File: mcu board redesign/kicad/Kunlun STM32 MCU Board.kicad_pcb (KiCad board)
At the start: 2 copper layers, 40 x 40 mm, 36 parts, among them J1 0532610671, J2 10129383-908001ALF, J3 USB4105-GF-A, J4 5002, J5 5002, J6 5002, J7 5002, J8 5001, J9 5001, SW1 KMR231NG ULC LFS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

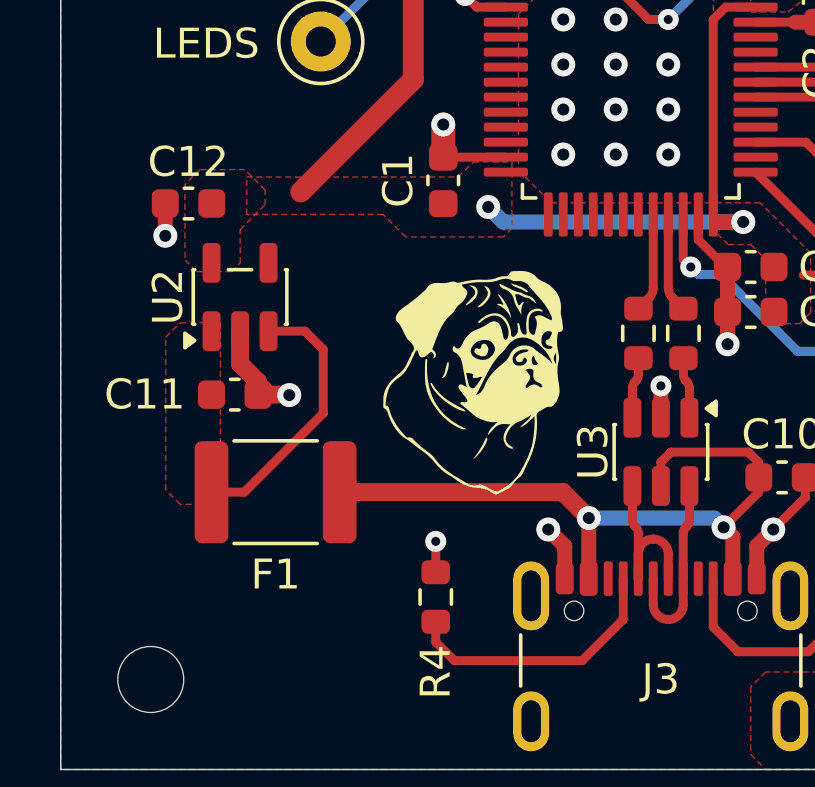
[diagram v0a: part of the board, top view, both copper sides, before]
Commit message: Added speaker, changed fuse.
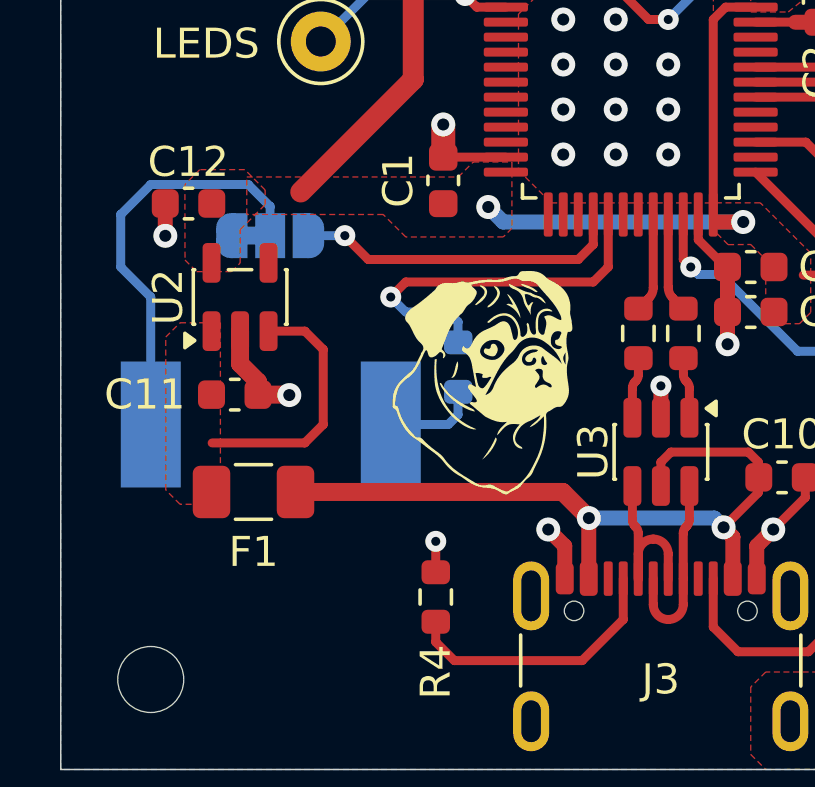
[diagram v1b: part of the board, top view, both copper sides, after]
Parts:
- added JP1: SolderJumper_3_Bridged12, Jumper:SolderJumper-3_P1.3mm_Bridged12_RoundedPad1.0x1.5mm, B.Cu at (135.2, 107.0)
- added LS1: Speaker, Buzzer_Beeper:Buzzer_CUI_CPT-9019S-SMT, B.Cu at (135.2, 113.2)
- added R7: 100, Resistor_SMD:R_0603_1608Metric, B.Cu at (141.5, 111.3)
- F1: footprint Fuse:Fuse_1812_4532Metric -> Fuse:Fuse_1206_3216Metric
- moved F1 0.74 mm to (134.7, 115.5)
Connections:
- U1 pad 28: unconnected-(U1-PB15-Pad28) -> /SPKR_ALT
- U1 pad 29: unconnected-(U1-PA8-Pad29) -> /SPKR_OUT
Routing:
- net Net-(JP1-C): track 0.00 -> 14.1 mm
- net /SPKR_OUT: track 0.00 -> 12.6 mm, vias 0 -> 1
- net /SPKR_ALT: track 0.00 -> 11.0 mm, vias 0 -> 1
- net Net-(LS1-Pad1): track 0.00 -> 3.23 mm
- net VBUS: track 24.0 -> 25.5 mm
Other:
- board text added: "Kunlun STM32 MCU Board r1"
- board text added: "by project 802"
- board text removed: "project 802 Kunlun STM32 MCU Board"
- board text removed: "r1"

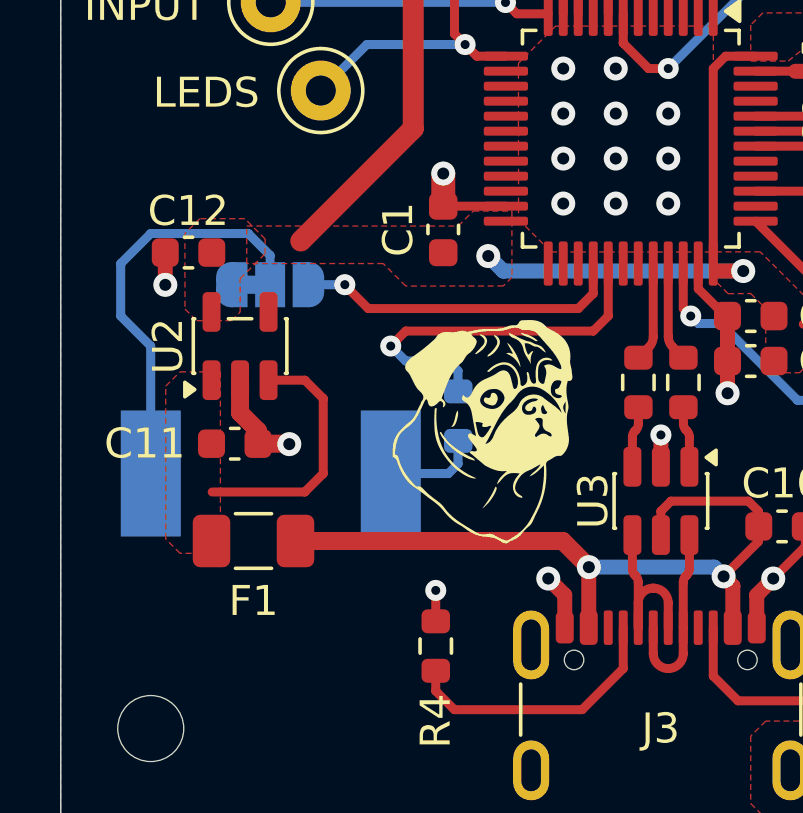
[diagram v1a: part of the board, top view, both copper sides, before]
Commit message: Slide power section closer to MCU
And associated layout tweaks
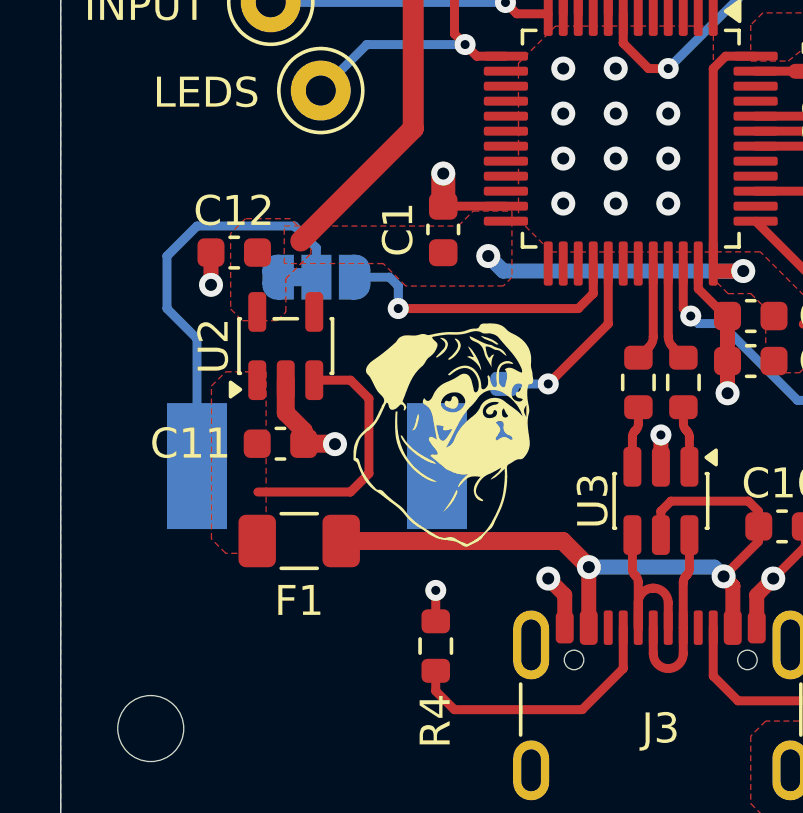
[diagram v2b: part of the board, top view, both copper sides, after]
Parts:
- moved JP1 1.56 mm to (136.8, 106.7)
- moved LS1 1.56 mm to (136.8, 113.0)
- moved R7 1.56 mm to (143.0, 111.1)
- moved C11 1.52 mm to (135.6, 112.3)
- moved C12 1.52 mm to (134.0, 105.9)
- moved F1 1.52 mm to (136.2, 115.5)
- moved U2 1.52 mm to (135.8, 109.0)
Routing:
- net /SPKR_OUT: track 12.6 -> 6.30 mm
- net VBUS: track 25.5 -> 23.9 mm
- net /SPKR_ALT: track 11.0 -> 10.0 mm

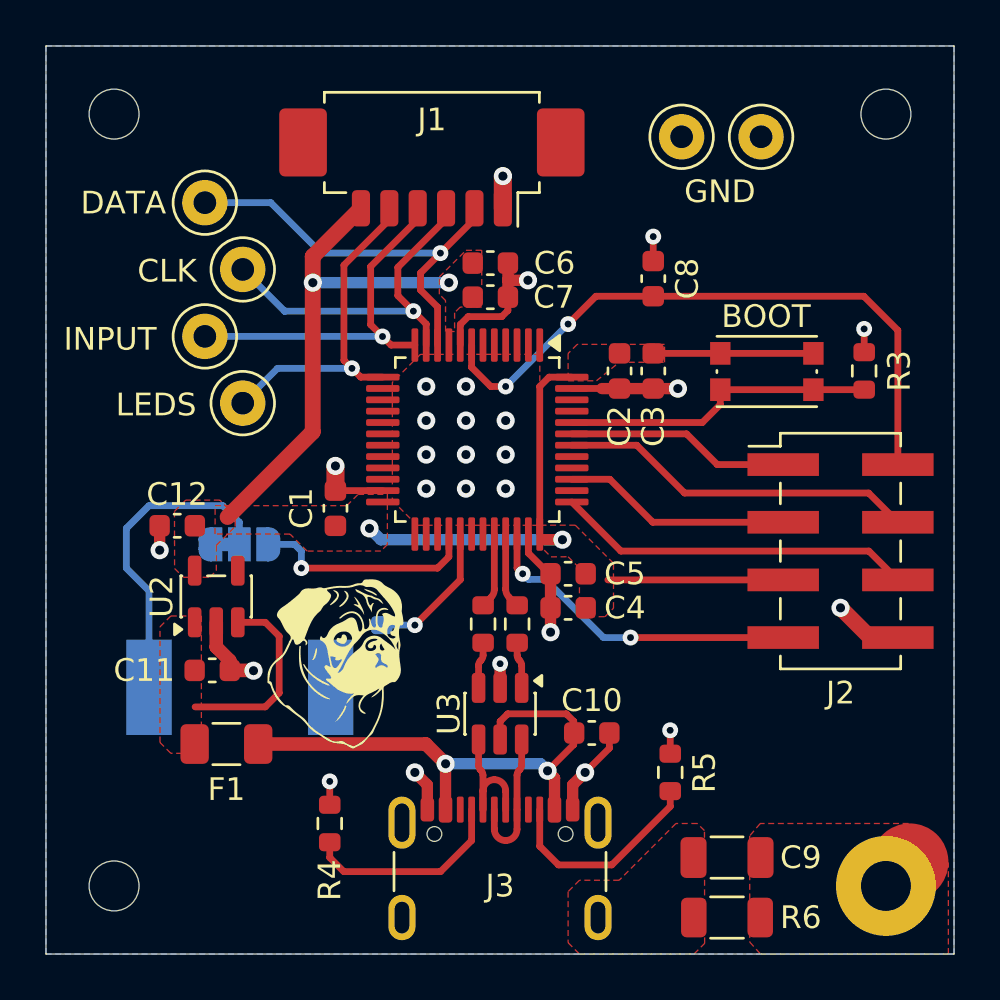
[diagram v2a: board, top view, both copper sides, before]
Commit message: Add a TVS to ESD circuit
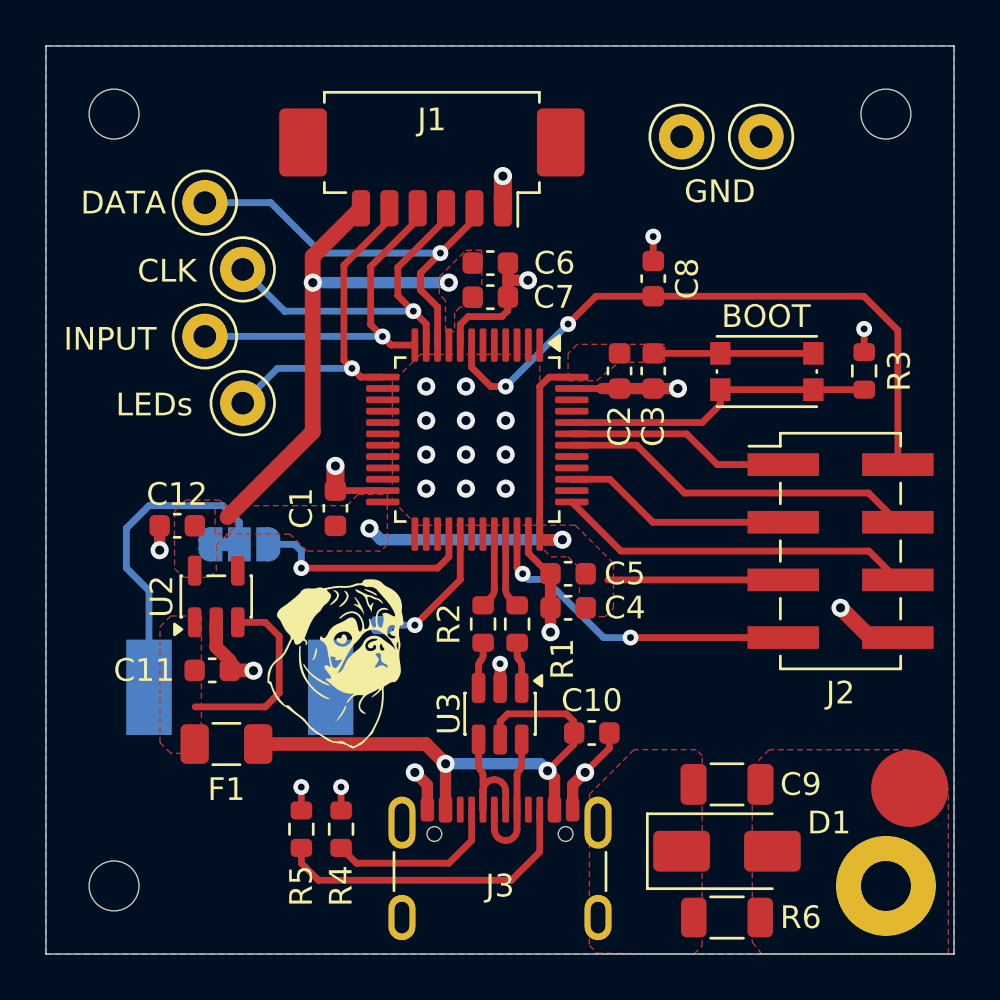
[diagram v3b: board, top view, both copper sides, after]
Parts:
- added D1: SMAJ5.0CA, Diode_SMD:D_SMA, F.Cu at (158.2, 120.2)
- moved R5 16.4 mm to (139.5, 119.2)
- moved C9 3.22 mm to (158.2, 117.3)
- moved R4 0.56 mm to (141.2, 119.2)
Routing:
- net Net-(J3-CC2): track 9.45 -> 13.9 mm
- net Net-(J3-CC1): track 9.11 -> 7.81 mm
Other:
- board text added: "LEDs"
- board text removed: "LEDS"

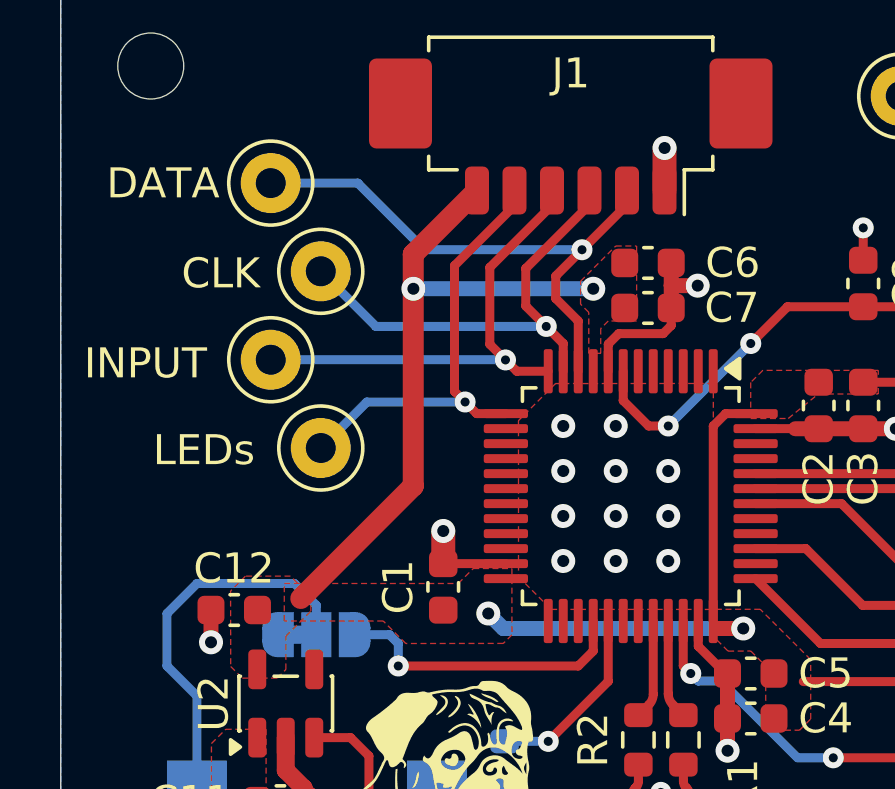
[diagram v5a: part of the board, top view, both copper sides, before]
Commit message: Move one trace a bit for cosmetics
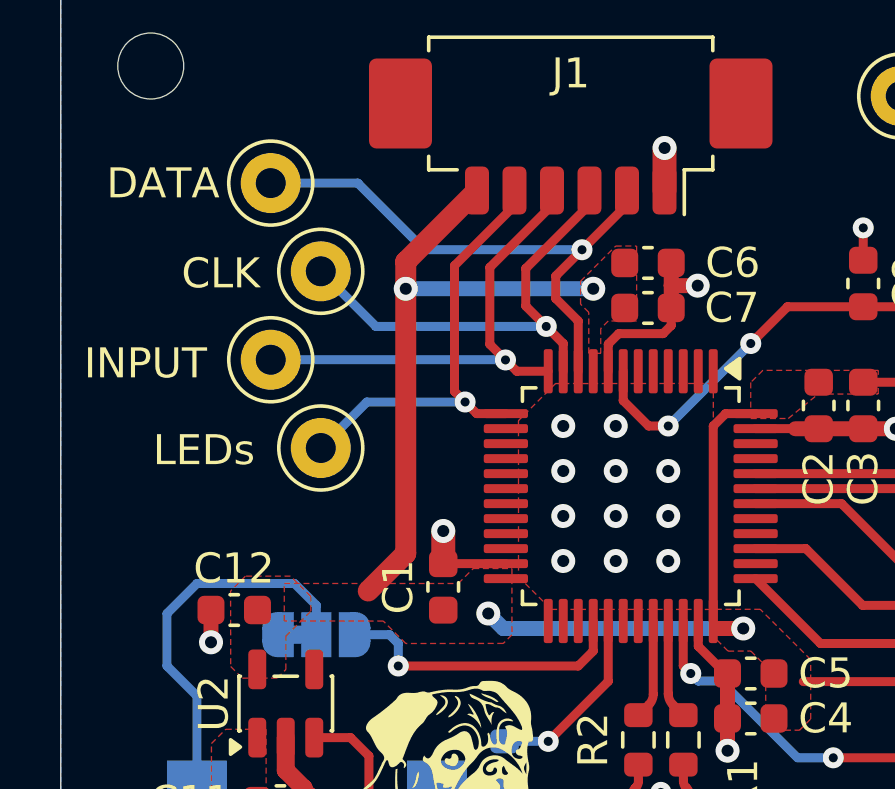
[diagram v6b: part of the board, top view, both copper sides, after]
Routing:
- net +3.3V: track 54.4 -> 53.5 mm
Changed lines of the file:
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@@
 	)
 	(segment
-		(start 142.125 91.9)
-		(end 140 94.025)
+		(start 139.75 104)
+		(end 138.5 105.25)
+		(width 0.7)
+		(layer "F.Cu")
+		(net "+3.3V")
+	)
+	(segment
+		(start 139.75 95.175739)
+		(end 139.75 104)
 		(width 0.7)
 		(layer "F.Cu")
@@
 		(end 157.953756 98.291629)
 		(width 0.3)
+		(layer "F.Cu")
+		(net "+3.3V")
+	)
+	(segment
+		(start 142.125 91.9)
+		(end 139.75 94.275)
+		(width 0.7)
+		(layer "F.Cu")
+		(net "+3.3V")
+	)
+	(segment
+		(start 139.75 94.275)
+		(end 139.75 95.175739)
+		(width 0.7)
 		(layer "F.Cu")
 		(net "+3.3V")
@@
 	)
 	(segment
-		(start 140 101.75)
-		(end 136.25 105.5)
-		(width 0.7)
-		(layer "F.Cu")
-		(net "+3.3V")
-	)
-	(segment
-		(start 140 94.025)
-		(end 140 101.75)
-		(width 0.7)
-		(layer "F.Cu")
-		(net "+3.3V")
-	)
-	(segment
 		(start 150.999156 106.499156)
 		(end 150.149945 106.499156)
@@
 	)
 	(via
-		(at 140.004009 95.175739)
+		(at 139.75 95.175739)
 		(size 0.8)
 		(drill 0.4)
@@
 	)
 	(segment
-		(start 140.004009 95.175739)
-		(end 146 95.175739)
+		(start 151 106.5)
+		(end 143 106.5)
 		(width 0.5)
 		(layer "B.Cu")
@@
 	)
 	(segment
-		(start 151 106.5)
-		(end 143 106.5)
+		(start 139.75 95.175739)
+		(end 146 95.175739)
 		(width 0.5)
 		(layer "B.Cu")
